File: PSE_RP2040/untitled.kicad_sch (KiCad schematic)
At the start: 19 parts

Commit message: schematico completato
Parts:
- added C?: (no value), symbol Device:C_Polarized
- D?: value (none) -> D
- L?: value (none) -> L
- R?: value (none) -> 33k
- R?: value (none) -> 10k
- U?: value (none) -> LMR16006YQ; footprint (none) -> Package_TO_SOT_SMD:SOT-23-6
- U?: value (none) -> TPS2375-1; footprint (none) -> Package_SO:TSSOP-8_4.4x3mm_P0.65mm
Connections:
- net GND: now also C?.2
- net poe-: now also R?.2
- net +3V3: now reaches C?.1, C?.1, L?.2, R?.1
- net +3V3: now also C?.1
- net at U?.1 (ILIM): now also R?.1
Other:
- note added: "PoE"
- note added: "Vref interna = 0,765"
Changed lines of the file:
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@@
   (junction (at 46.99 69.85) (diameter 0) (color 0 0 0 0)
   )
+  (junction (at 261.62 50.8) (diameter 0) (color 0 0 0 0)
+  )
   (junction (at 152.4 45.72) (diameter 0) (color 0 0 0 0)
   )
@@
   (junction (at 142.24 45.72) (diameter 0) (color 0 0 0 0)
   )
+  (junction (at 59.69 87.63) (diameter 0) (color 0 0 0 0)
+  )
   (junction (at 66.04 87.63) (diameter 0) (color 0 0 0 0)
   )
   (junction (at 199.39 50.8) (diameter 0) (color 0 0 0 0)
   )
+  (junction (at 271.78 50.8) (diameter 0) (color 0 0 0 0)
+  )
   (wire (pts (xy 59.69 59.69) (xy 66.04 59.69))
     (stroke (width 0) (type default) (color 0 0 0 0))
@@
     (stroke (width 0) (type default) (color 0 0 0 0))
   )
+  (wire (pts (xy 59.69 87.63) (xy 46.99 87.63))
+    (stroke (width 0) (type default) (color 0 0 0 0))
+  )
   (wire (pts (xy 189.23 45.72) (xy 189.23 31.75))
     (stroke (width 0) (type default) (color 0 0 0 0))
@@
     (stroke (width 0) (type default) (color 0 0 0 0))
   )
+  (wire (pts (xy 271.78 50.8) (xy 271.78 53.34))
+    (stroke (width 0) (type default) (color 0 0 0 0))
+  )
   (wire (pts (xy 31.75 45.72) (xy 46.99 45.72))
     (stroke (width 0) (type default) (color 0 0 0 0))
@@
     (stroke (width 0) (type default) (color 0 0 0 0))
   )
+  (wire (pts (xy 59.69 69.85) (xy 59.69 62.23))
+    (stroke (width 0) (type default) (color 0 0 0 0))
+  )
+  (wire (pts (xy 59.69 62.23) (xy 72.39 62.23))
+    (stroke (width 0) (type default) (color 0 0 0 0))
+  )
   (wire (pts (xy 46.99 87.63) (xy 46.99 69.85))
     (stroke (width 0) (type default) (color 0 0 0 0))
@@
     (stroke (width 0) (type default) (color 0 0 0 0))
   )
+  (wire (pts (xy 261.62 50.8) (xy 271.78 50.8))
+    (stroke (width 0) (type default) (color 0 0 0 0))
+  )
   (wire (pts (xy 59.69 45.72) (xy 66.04 45.72))
     (stroke (width 0) (type default) (color 0 0 0 0))
@@
     (stroke (width 0) (type default) (color 0 0 0 0))
   )
-  (wire (pts (xy 66.04 87.63) (xy 46.99 87.63))
+  (wire (pts (xy 66.04 87.63) (xy 59.69 87.63))
     (stroke (width 0) (type default) (color 0 0 0 0))
   )
@@
   (wire (pts (xy 82.55 52.07) (xy 82.55 45.72))
     (stroke (width 0) (type default) (color 0 0 0 0))
+  )
+  (wire (pts (xy 59.69 77.47) (xy 59.69 87.63))
+    (stroke (width 0) (type default) (color 0 0 0 0))
+  )
+  (text "Vref interna = 0,765" (at 227.33 63.5 0)
+    (effects (font (size 1.27 1.27)) (justify left bottom))
+  )
+  (text "PoE\n" (at 16.51 16.51 0)
+    (effects (font (size 1.27 1.27)) (justify left bottom))
   )
   (global_label "poe-" (shape input) (at 31.75 69.85 180) (fields_autoplaced)
@@
       (effects (font (size 1.27 1.27)) (justify left))
     )
-    (property "Value" "" (id 1) (at 225.298 57.5822 0)
+    (property "Value" "33k" (id 1) (at 225.298 57.5822 0)
       (effects (font (size 1.27 1.27)) (justify left))
     )
@@
     (in_bom yes) (on_board yes) (fields_autoplaced)
     (property "Reference" "U?" (id 0) (at 171.45 39.4802 0))
-    (property "Value" "" (id 1) (at 171.45 42.0171 0))
-    (property "Footprint" "" (id 2) (at 171.45 63.5 0)
+    (property "Value" "LMR16006YQ" (id 1) (at 171.45 42.0171 0))
+    (property "Footprint" "Package_TO_SOT_SMD:SOT-23-6" (id 2) (at 171.45 63.5 0)
       (effects (font (size 1.27 1.27) italic) hide)
     )
@@
     (pin "6")
   )
+  (symbol (lib_id "power:+3.3V") (at 271.78 50.8 0) (unit 1)
+    (in_bom yes) (on_board yes) (fields_autoplaced)
+    (property "Reference" "#PWR?" (id 0) (at 271.78 54.61 0)
+      (effects (font (size 1.27 1.27)) hide)
+    )
+    (property "Value" "" (id 1) (at 271.78 47.2242 0))
+    (property "Footprint" "" (id 2) (at 271.78 50.8 0)
+      (effects (font (size 1.27 1.27)) hide)
+    )
+    (property "Datasheet" "" (id 3) (at 271.78 50.8 0)
+      (effects (font (size 1.27 1.27)) hide)
+    )
+    (pin "1")
+  )
   (symbol (lib_id "Device:R") (at 66.04 73.66 0) (unit 1)
     (in_bom yes) (on_board yes) (fields_autoplaced)
@@
       (effects (font (size 1.27 1.27)) (justify left))
     )
-    (property "Value" "" (id 1) (at 225.298 67.7422 0)
+    (property "Value" "10k" (id 1) (at 225.298 67.7422 0)
       (effects (font (size 1.27 1.27)) (justify left))
     )
@@
     )
     (property "Datasheet" "~" (id 3) (at 59.69 52.07 0)
+      (effects (font (size 1.27 1.27)) hide)
+    )
+    (pin "1")
+    (pin "2")
+  )
+  (symbol (lib_id "Device:C_Polarized") (at 271.78 57.15 0) (unit 1)
+    (in_bom yes) (on_board yes) (fields_autoplaced)
+    (property "Reference" "C?" (id 0) (at 274.701 55.4263 0)
+      (effects (font (size 1.27 1.27)) (justify left))
+    )
+    (property "Value" "" (id 1) (at 274.701 57.9632 0)
+      (effects (font (size 1.27 1.27)) (justify left))
+    )
+    (property "Footprint" "" (id 2) (at 272.7452 60.96 0)
+      (effects (font (size 1.27 1.27)) hide)
+    )
+    (property "Datasheet" "~" (id 3) (at 271.78 57.15 0)
       (effects (font (size 1.27 1.27)) hide)
     )
@@
       (effects (font (size 1.27 1.27)) (justify left))
     )
-    (property "Value" "" (id 1) (at 84.5694 53.4471 0)
-      (effects (font (size 1.27 1.27)) (justify left))
-    )
-    (property "Footprint" "" (id 2) (at 82.55 82.55 0)
+    (property "Value" "TPS2375-1" (id 1) (at 84.5694 53.4471 0)
+      (effects (font (size 1.27 1.27)) (justify left))
+    )
+    (property "Footprint" "Package_SO:TSSOP-8_4.4x3mm_P0.65mm" (id 2) (at 82.55 82.55 0)
       (effects (font (size 1.27 1.27)) hide)
     )
@@
     (pin "1")
   )
+  (symbol (lib_id "power:GND") (at 271.78 60.96 0) (unit 1)
+    (in_bom yes) (on_board yes) (fields_autoplaced)
+    (property "Reference" "#PWR?" (id 0) (at 271.78 67.31 0)
+      (effects (font (size 1.27 1.27)) hide)
+    )
+    (property "Value" "" (id 1) (at 271.78 65.4034 0))
+    (property "Footprint" "" (id 2) (at 271.78 60.96 0)
+      (effects (font (size 1.27 1.27)) hide)
+    )
+    (property "Datasheet" "" (id 3) (at 271.78 60.96 0)
+      (effects (font (size 1.27 1.27)) hide)
+    )
+    (pin "1")
+  )
   (symbol (lib_id "Device:C") (at 236.22 55.88 0) (unit 1)
     (in_bom yes) (on_board yes) (fields_autoplaced)
@@
     (in_bom yes) (on_board yes) (fields_autoplaced)
     (property "Reference" "L?" (id 0) (at 212.09 46.5922 90))
-    (property "Value" "" (id 1) (at 212.09 49.1291 90))
+    (property "Value" "L" (id 1) (at 212.09 49.1291 90))
     (property "Footprint" "" (id 2) (at 212.09 50.8 0)
       (effects (font (size 1.27 1.27)) hide)
@@
       (effects (font (size 1.27 1.27)) hide)
     )
-    (property "Value" "" (id 1) (at 129.54 73.0234 0))
+    (property "Value" "GND" (id 1) (at 129.54 73.0234 0))
     (property "Footprint" "" (id 2) (at 129.54 68.58 0)
       (effects (font (size 1.27 1.27)) hide)
@@
     (in_bom yes) (on_board yes) (fields_autoplaced)
     (property "Reference" "D?" (id 0) (at 111.76 40.7502 0))
-    (property "Value" "" (id 1) (at 111.76 43.2871 0))
+    (property "Value" "D" (id 1) (at 111.76 43.2871 0))
     (property "Footprint" "" (id 2) (at 111.76 45.72 0)
       (effects (font (size 1.27 1.27)) hide)

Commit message: rtc aggiunta
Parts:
- added C?: 100n, symbol Device:C
- added C? (x2): 47u, symbol Device:C
- added C?: 1u, symbol Device:C
- added D? (x2): MBR1020VL, Diode_SMD:D_SOD-123F, symbol Diode:MBR1020VL
- added L?: 2U2, symbol Device:L
- added R? (x2): 100k, symbol Device:R
- added U?: MCP1703A-3302_SOT23, Package_TO_SOT_SMD:SOT-23, symbol Regulator_Linear:MCP1703A-3302_SOT23
- added U?: RT6150A_B, symbol PSE_RP2040-rescue:RT6150A_B-buck_converter
- C? (x2): value (none) -> 100n
- C?: value (none) -> 100u
- C? (x2): value (none) -> 2u2
- C? (x2): value (none) -> 100n 100v
- C?: value (none) -> 470p
- R?: value (none) -> 330
- R? (x2): value (none) -> 50k
- R?: value (none) -> 27
- R?: value (none) -> 178k
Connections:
- net +3V3: now also C?.1, C?.1, U?.1 (VOUT), U?.10 (FB), U?.2 (VO)
- net GND: now also C?.2, C?.2, C?.2, C?.2, R?.2, U?.1 (GND), U?.11 (GND_PAD), U?.3 (GND), U?.9 (GND)
- new net: C?.1, D?.1 (K), R?.1, U?.5 (VIN), U?.8 (VINA)
- new net: C?.1, D?.1 (K), U?.3 (VI)
- new net: L?.2, U?.2 (LX2)
- new net: L?.1, U?.4 (LX1)
- new net +5V: D?.2 (A), D?.2 (A)
- new net GPIO23: R?.1, U?.7 (PS)
- new net SHUT_DOWN: R?.2, U?.6 (EN)
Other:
- note added: "power"
- note removed: "PoE"

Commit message: Presentazione
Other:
- note added: "Alimentazioi"
- note added: "POE"
- note removed: "power"
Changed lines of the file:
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@@
+    (stroke (width 0) (type default) (color 0 0 0 0))
+  )
+  (polyline (pts (xy 11.43 90.17) (xy 284.48 90.17))
     (stroke (width 0) (type default) (color 0 0 0 0))
   )
@@
     (effects (font (size 1.27 1.27)) (justify left bottom))
   )
-  (text "power\n" (at 16.51 16.51 0)
+  (text "POE" (at 16.51 16.51 0)
     (effects (font (size 1.27 1.27)) (justify left bottom))
   )
+  (text "Alimentazioi" (at 17.78 96.52 0)
+    (effects (font (size 1.27 1.27)) (justify left bottom))
+  )

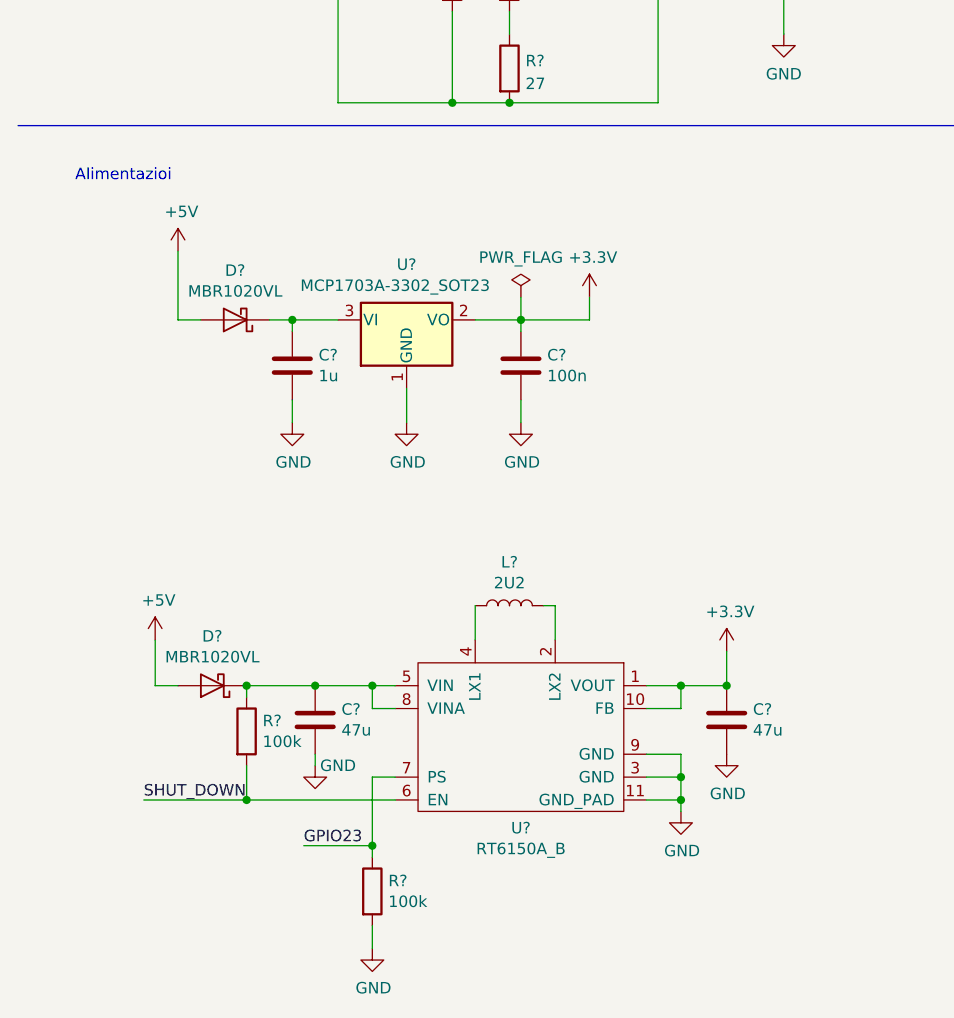
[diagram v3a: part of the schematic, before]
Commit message: modifiche schematico
cancellata sezione alimentazione non più necessaria (usiamo switching del poe)
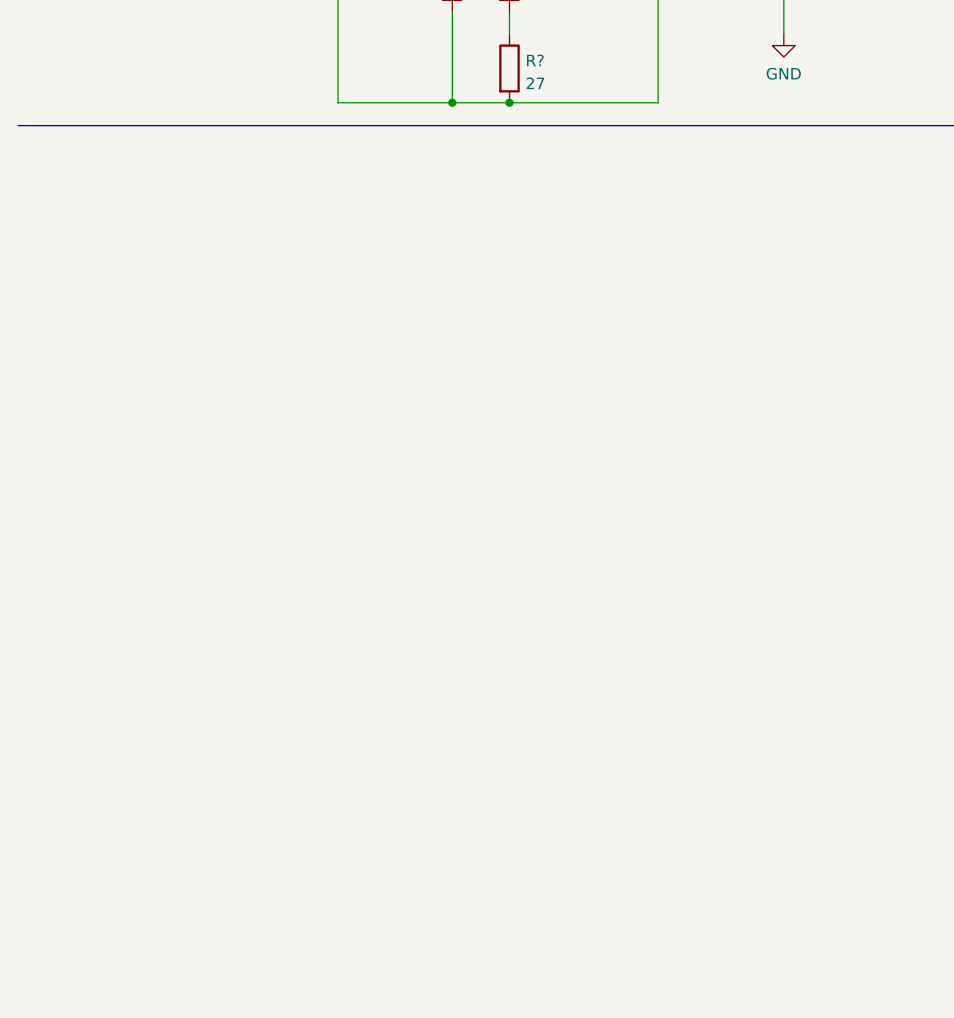
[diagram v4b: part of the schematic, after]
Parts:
- removed C?: 100n, symbol Device:C
- removed C? (x2): 47u, symbol Device:C
- removed C?: 1u, symbol Device:C
- removed D? (x2): MBR1020VL, Diode_SMD:D_SOD-123F, symbol Diode:MBR1020VL
- removed L?: 2U2, symbol Device:L
- removed R? (x2): 100k, symbol Device:R
- removed U?: MCP1703A-3302_SOT23, Package_TO_SOT_SMD:SOT-23, symbol Regulator_Linear:MCP1703A-3302_SOT23
- removed U?: RT6150A_B, symbol PSE_RP2040-rescue:RT6150A_B-buck_converter
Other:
- note removed: "Alimentazioi"

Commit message: schematico
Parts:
- U?: value TPS2375-1 -> (none)
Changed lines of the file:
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@@
-    (stroke (width 0) (type default) (color 0 0 0 0))
-  )
-  (polyline (pts (xy 11.43 90.17) (xy 284.48 90.17))
     (stroke (width 0) (type default) (color 0 0 0 0))
   )
@@
       (effects (font (size 1.27 1.27)) (justify left))
     )
-    (property "Value" "TPS2375-1" (id 1) (at 84.5694 53.4471 0)
-      (effects (font (size 1.27 1.27)) (justify left))
-    )
+    (property "Value" "" (id 1) (at 84.5694 53.4471 0)
+      (effects (font (size 1.27 1.27)) (justify left))
+    )

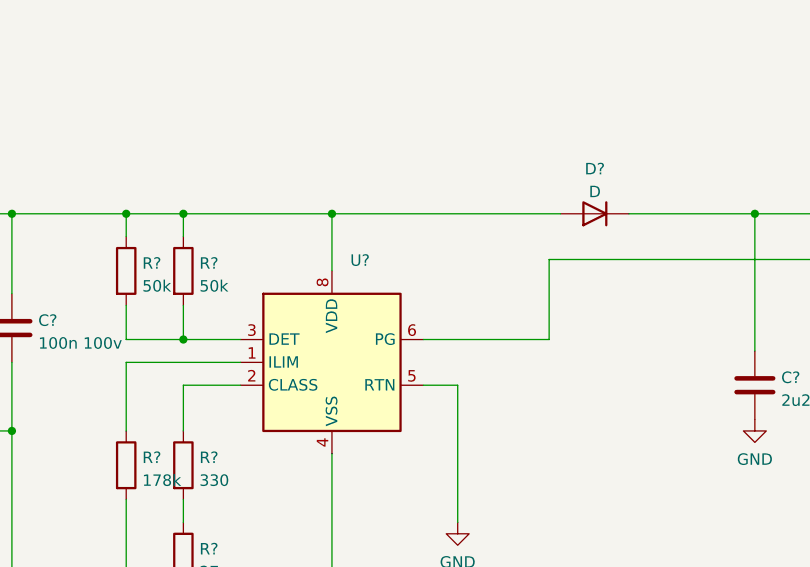
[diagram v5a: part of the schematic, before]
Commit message: schematico rtc
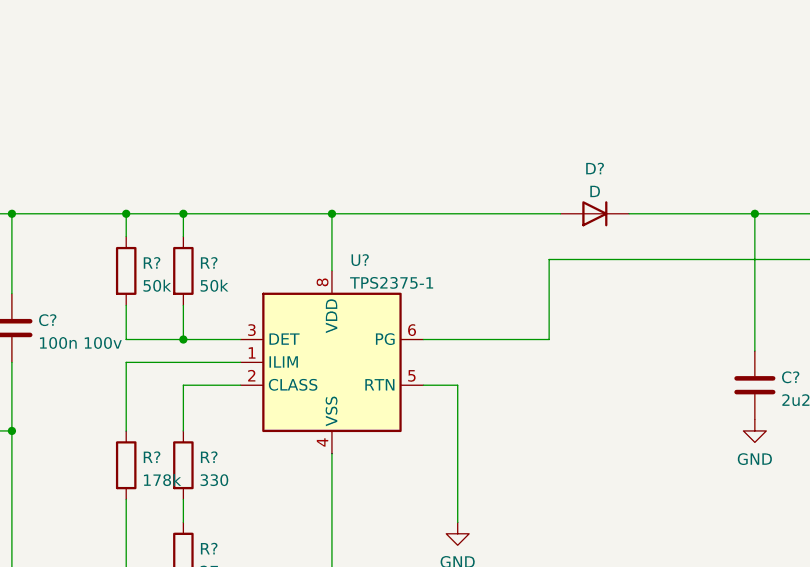
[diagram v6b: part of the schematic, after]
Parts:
- U?: value (none) -> TPS2375-1
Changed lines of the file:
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@@
   (symbol (lib_id "power:+3.3V") (at 271.78 50.8 0) (unit 1)
     (in_bom yes) (on_board yes) (fields_autoplaced)
-    (property "Reference" "#PWR?" (id 0) (at 271.78 54.61 0)
+    (property "Reference" "#PWR0183" (id 0) (at 271.78 54.61 0)
       (effects (font (size 1.27 1.27)) hide)
     )
@@
   (symbol (lib_id "power:GND") (at 171.45 60.96 0) (unit 1)
     (in_bom yes) (on_board yes) (fields_autoplaced)
-    (property "Reference" "#PWR?" (id 0) (at 171.45 67.31 0)
+    (property "Reference" "#PWR0190" (id 0) (at 171.45 67.31 0)
       (effects (font (size 1.27 1.27)) hide)
     )
@@
       (effects (font (size 1.27 1.27)) (justify left))
     )
-    (property "Value" "" (id 1) (at 84.5694 53.4471 0)
+    (property "Value" "TPS2375-1" (id 1) (at 84.5694 53.4471 0)
       (effects (font (size 1.27 1.27)) (justify left))
     )
@@
   (symbol (lib_id "power:GND") (at 152.4 69.85 0) (unit 1)
     (in_bom yes) (on_board yes) (fields_autoplaced)
-    (property "Reference" "#PWR?" (id 0) (at 152.4 76.2 0)
+    (property "Reference" "#PWR0188" (id 0) (at 152.4 76.2 0)
       (effects (font (size 1.27 1.27)) hide)
     )
@@
   (symbol (lib_id "power:GND") (at 199.39 60.96 0) (unit 1)
     (in_bom yes) (on_board yes) (fields_autoplaced)
-    (property "Reference" "#PWR?" (id 0) (at 199.39 67.31 0)
+    (property "Reference" "#PWR0186" (id 0) (at 199.39 67.31 0)
       (effects (font (size 1.27 1.27)) hide)
     )
@@
   (symbol (lib_id "power:GND") (at 261.62 73.66 0) (unit 1)
     (in_bom yes) (on_board yes) (fields_autoplaced)
-    (property "Reference" "#PWR?" (id 0) (at 261.62 80.01 0)
+    (property "Reference" "#PWR0182" (id 0) (at 261.62 80.01 0)
       (effects (font (size 1.27 1.27)) hide)
     )
@@
   (symbol (lib_id "power:GND") (at 271.78 60.96 0) (unit 1)
     (in_bom yes) (on_board yes) (fields_autoplaced)
-    (property "Reference" "#PWR?" (id 0) (at 271.78 67.31 0)
+    (property "Reference" "#PWR0184" (id 0) (at 271.78 67.31 0)
       (effects (font (size 1.27 1.27)) hide)
     )
@@
   (symbol (lib_id "power:GND") (at 142.24 68.58 0) (unit 1)
     (in_bom yes) (on_board yes) (fields_autoplaced)
-    (property "Reference" "#PWR?" (id 0) (at 142.24 74.93 0)
+    (property "Reference" "#PWR0189" (id 0) (at 142.24 74.93 0)
       (effects (font (size 1.27 1.27)) hide)
     )
@@
   (symbol (lib_id "power:GND") (at 223.52 69.85 0) (unit 1)
     (in_bom yes) (on_board yes) (fields_autoplaced)
-    (property "Reference" "#PWR?" (id 0) (at 223.52 76.2 0)
+    (property "Reference" "#PWR0181" (id 0) (at 223.52 76.2 0)
       (effects (font (size 1.27 1.27)) hide)
     )
@@
   (symbol (lib_id "power:GND") (at 129.54 68.58 0) (unit 1)
     (in_bom yes) (on_board yes) (fields_autoplaced)
-    (property "Reference" "#PWR?" (id 0) (at 129.54 74.93 0)
+    (property "Reference" "#PWR0187" (id 0) (at 129.54 74.93 0)
       (effects (font (size 1.27 1.27)) hide)
     )
@@
   (symbol (lib_id "power:GND") (at 96.52 80.01 0) (unit 1)
     (in_bom yes) (on_board yes) (fields_autoplaced)
-    (property "Reference" "#PWR?" (id 0) (at 96.52 86.36 0)
-      (effects (font (size 1.27 1.27)) hide)
-    )
+    (property "Reference" "#PWR0185" (id 0) (at 96.52 86.36 0)
+      (effects (font (size 1.27 1.27)) hide)
+    )

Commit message: aggiornamento schematico
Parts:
- added JP1: (no value), symbol Jumper:SolderJumper_2_Bridged
- gave numbers to parts that had none: 20
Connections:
- net at U8.4 (~{SHDN}): now also JP1.2 (B); no longer U7.6 (PG)
- new net: JP1.1 (A), U7.6 (PG)
